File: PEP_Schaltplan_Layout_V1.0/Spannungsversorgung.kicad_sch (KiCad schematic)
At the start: 21 parts, among them Q3 BC546, Q4 BC556, U12 AD822ANZ_new, U23 LM7905_TO220, U24 LM7805_TO220

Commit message: alle_Bauteile
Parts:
- added D7, D8, D9: LED, LED_THT:LED_D3.0mm, symbol Device:LED
- added R29, R30: 470, Resistor_SMD:R_1206_3216Metric, symbol ltspice:res
- added R36: 2k2, Resistor_SMD:R_1206_3216Metric, symbol ltspice:res
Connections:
- net +5V: now also R29.1
- net +7.5V: now also R36.1
- net -5V: now also R30.2
- net -7.5V: now also D9.1 (K)
- net GND: now also D7.1 (K), D8.1 (K)
- new net: D9.2 (A), R36.2
- new net: D7.2 (A), R30.1
- new net: D8.2 (A), R29.2

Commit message: lol
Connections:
- net at Q3.2 (B), U12.1: now also Q4.2 (B)
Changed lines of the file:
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@@
+	)
+	(junction
+		(at 114.3 100.33)
+		(diameter 0)
+		(color 0 0 0 0)
 	)
 	(junction
@@
 		)
 		(stroke
+			(width 0)
+			(type default)
+		)
+	)
+	(wire
+		(pts
+			(xy 114.3 100.33) (xy 114.3 107.95)
+		)
+		(stroke

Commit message: Überarbeitung und Bereinigung
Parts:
- C2: renamed from C16; footprint (none) -> Capacitor_SMD:C_1206_3216Metric
- renumbered C15 to C1, C17 to C3, C18 to C4, C19 to C5, C20 to C6, C21 to C7, C22 to C8, D9 to D1, D13 to D2, D14 to D3, D15 to D4, D16 to D5, D8 to D6, Q3 to Q1, Q4 to Q2, R36 to R1, R25 to R2, R26 to R3, R45 to R4, R49 to R5, R29 to R6, R30 to R7, U12 to U1, U24 to U2, U23 to U3
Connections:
- net -7.5V: now also C4.2
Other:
- moved on the sheet: C1, C2, C3, C4, C5, C6, C7, C8, D1, D2, D3, D4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

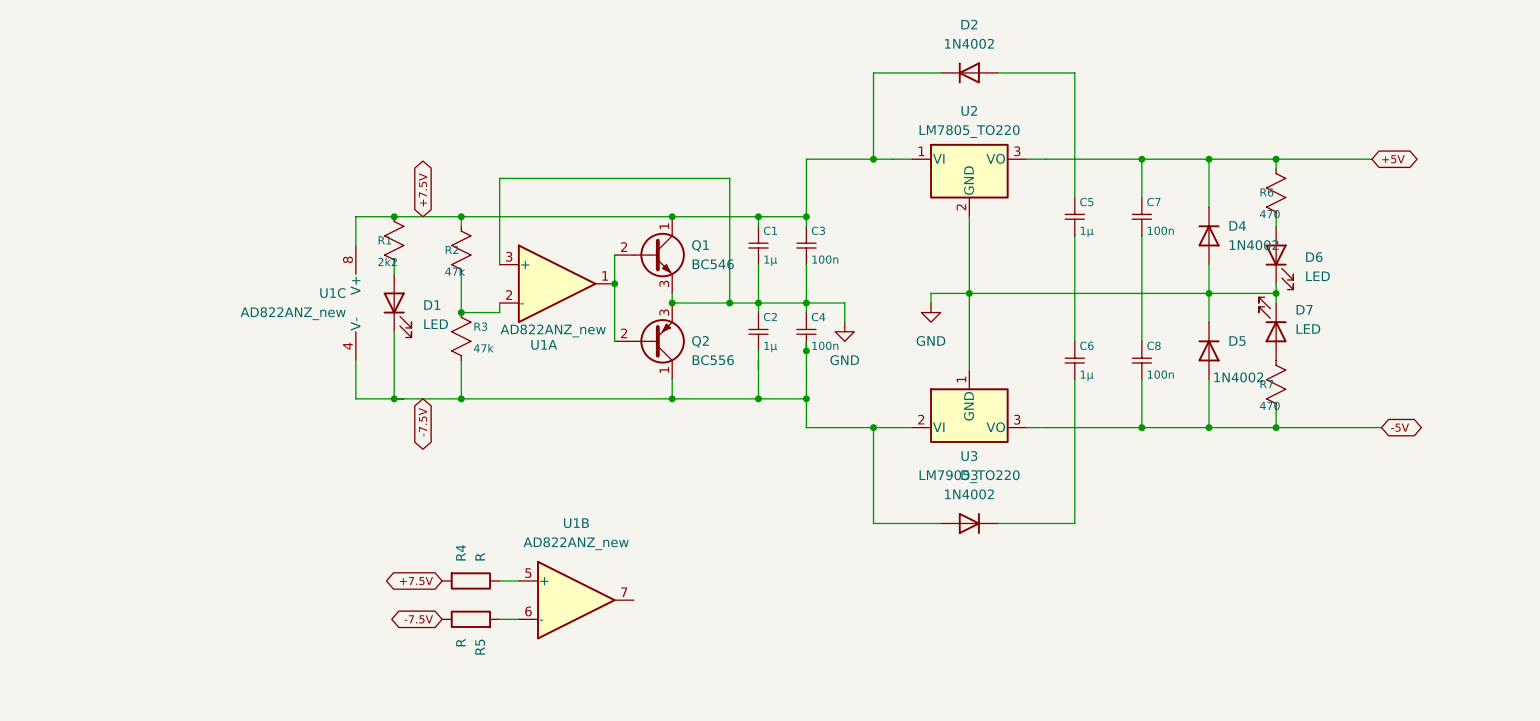
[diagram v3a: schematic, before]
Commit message: Pinheads eingefügt, GND überall (hoffentlich angebunden)
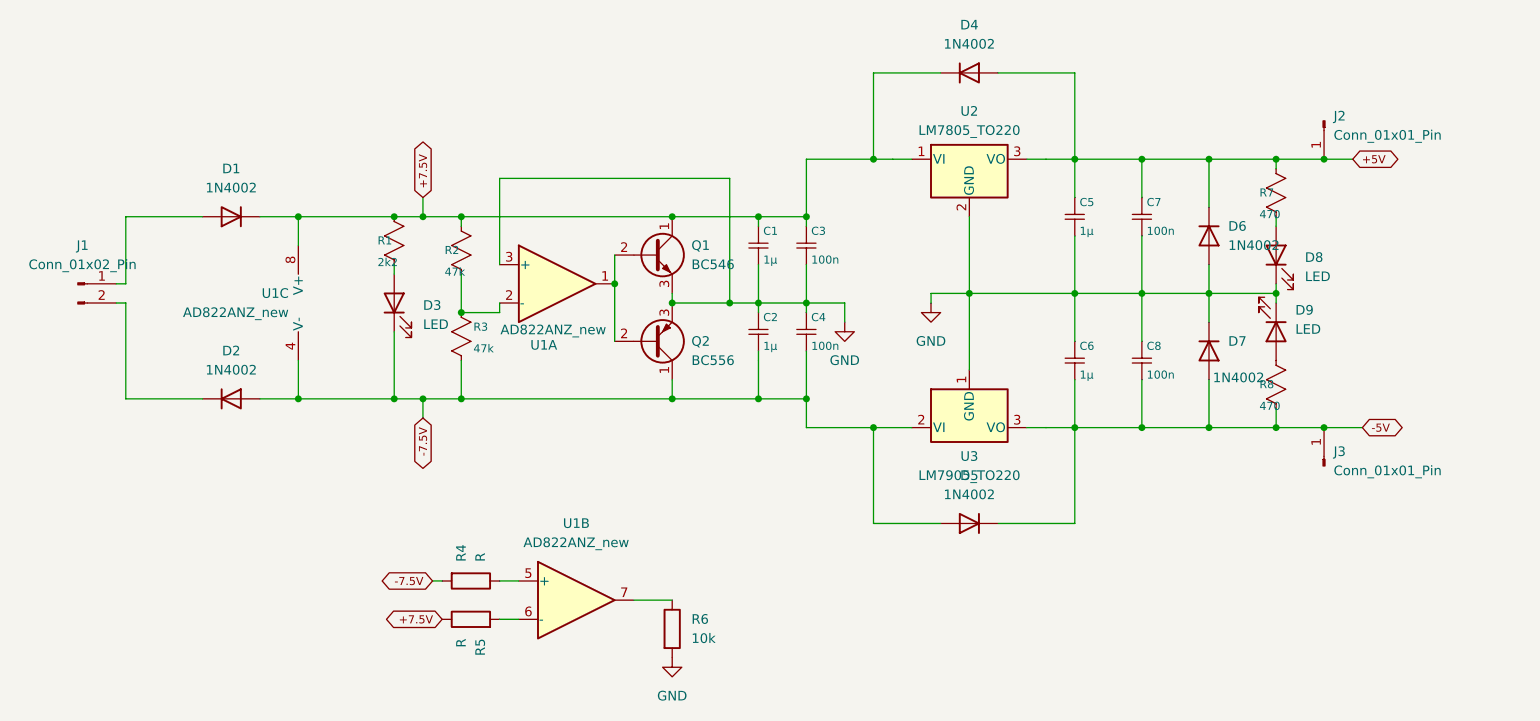
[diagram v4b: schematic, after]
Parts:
- added D1, D2: 1N4002, Diode_THT:D_DO-41_SOD81_P10.16mm_Horizontal, symbol Diode:1N4002
- added J1: Conn_01x02_Pin, Connector_PinHeader_2.54mm:PinHeader_1x02_P2.54mm_Vertical, symbol Connector:Conn_01x02_Pin
- added J2, J3: Conn_01x01_Pin, Connector_PinSocket_2.54mm:PinSocket_1x01_P2.54mm_Vertical, symbol Connector:Conn_01x01_Pin
- added R6: 10k, Resistor_SMD:R_1206_3216Metric, symbol Device:R
- renumbered D1 to D3, D2 to D4, D3 to D5, D4 to D6, D5 to D7, D6 to D8, D7 to D9, R6 to R7, R7 to R8
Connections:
- net +5V: now also C5.1, D4.2 (A), J2.1 (Pin_1)
- net +7.5V: now also R5.1, D1.1 (K); no longer R4.2
- net -5V: now also C6.2, D5.1 (K), J3.1 (Pin_1)
- net -7.5V: now also R4.2, D2.2 (A); no longer R5.1
- net GND: now also C5.2, C6.1, C7.2, C8.1, R6.2
- net at U1.7: now also R6.1
- new net: D1.2 (A), J1.1 (Pin_1)
- new net: D2.1 (K), J1.2 (Pin_2)
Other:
- moved on the sheet: U1C

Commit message: Anpassung
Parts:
- R4, R5: value R -> 2k2
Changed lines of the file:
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@@
 			)
 		)
-		(property "Value" "R"
+		(property "Value" "2k2"
 			(at 83.8199 129.54 0)
 			(show_name no)
@@
 			)
 		)
-		(property "Value" "R"
+		(property "Value" "2k2"
 			(at 81.2801 139.7 0)
 			(show_name no)
